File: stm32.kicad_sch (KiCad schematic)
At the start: 47 parts, among them J1 USB_B_Micro, J19 Conn_01x06, J2 Conn_02x05_Odd_Even, J7 TC2030, SW1 SW_Push, SW2 SW_Push, SW3 SW_Push, SW4 SW_Push, U1 STM32F427VGT6, U3 molex_48pin_MRE, U5 LM1117-3.3, X1 8MHz 20pF, Y2 32768 Hz

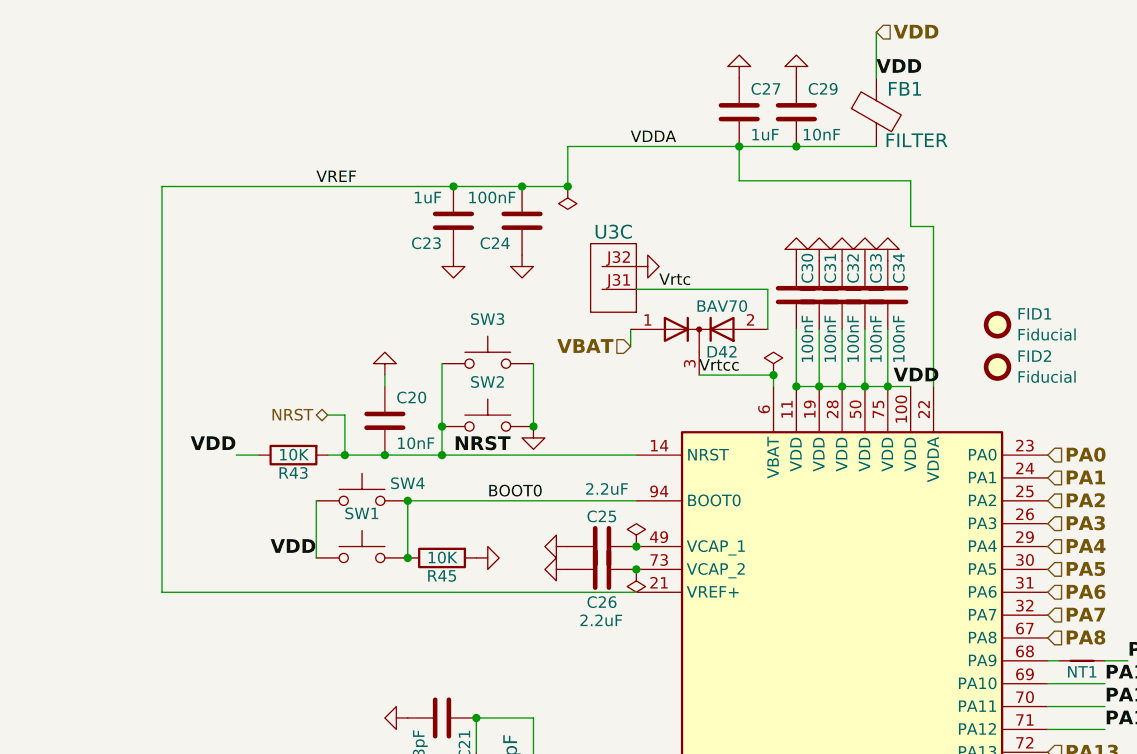
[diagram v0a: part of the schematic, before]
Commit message: added JP6
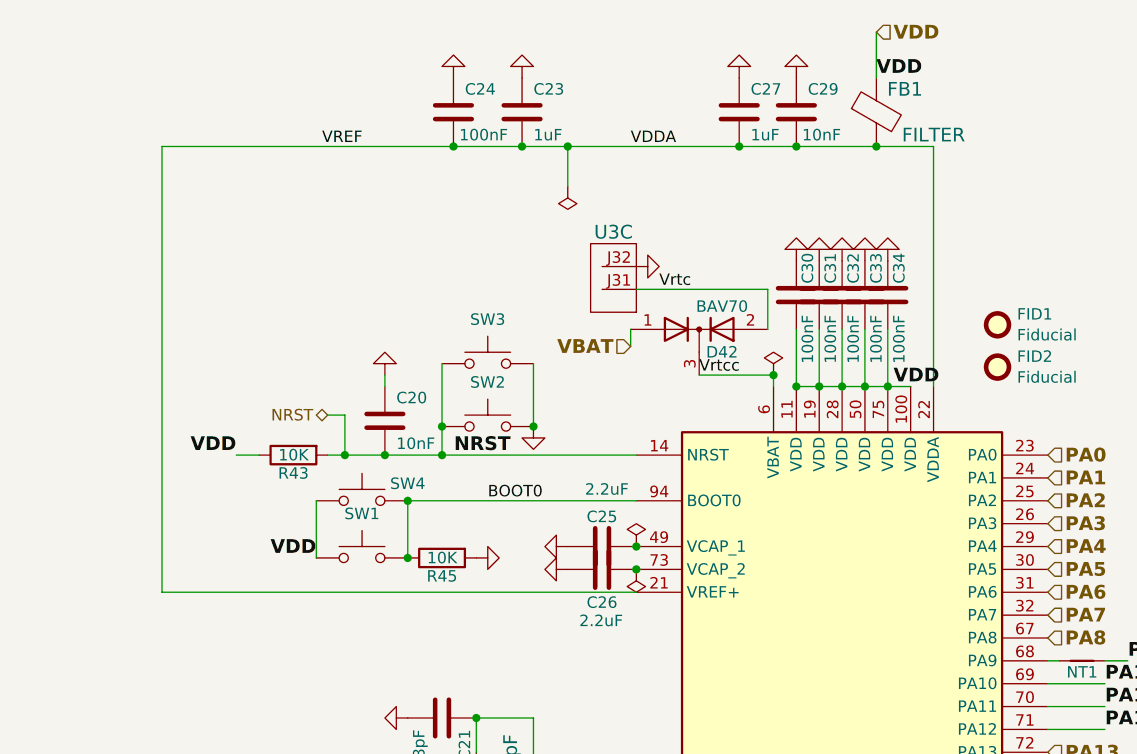
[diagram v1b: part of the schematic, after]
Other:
- moved on the sheet: C23, C24
